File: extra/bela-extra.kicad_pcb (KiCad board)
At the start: 2 copper layers, 84 parts, among them P1 bbp9, P10 GU128x64E-U100, P11 gui140x16j-7002, P12 digital_in, P13 digital_out, P2 bbbp8, P3 enc+btn1, P4 enc+btn2, P5 MTA-156-4, P6 bela_power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

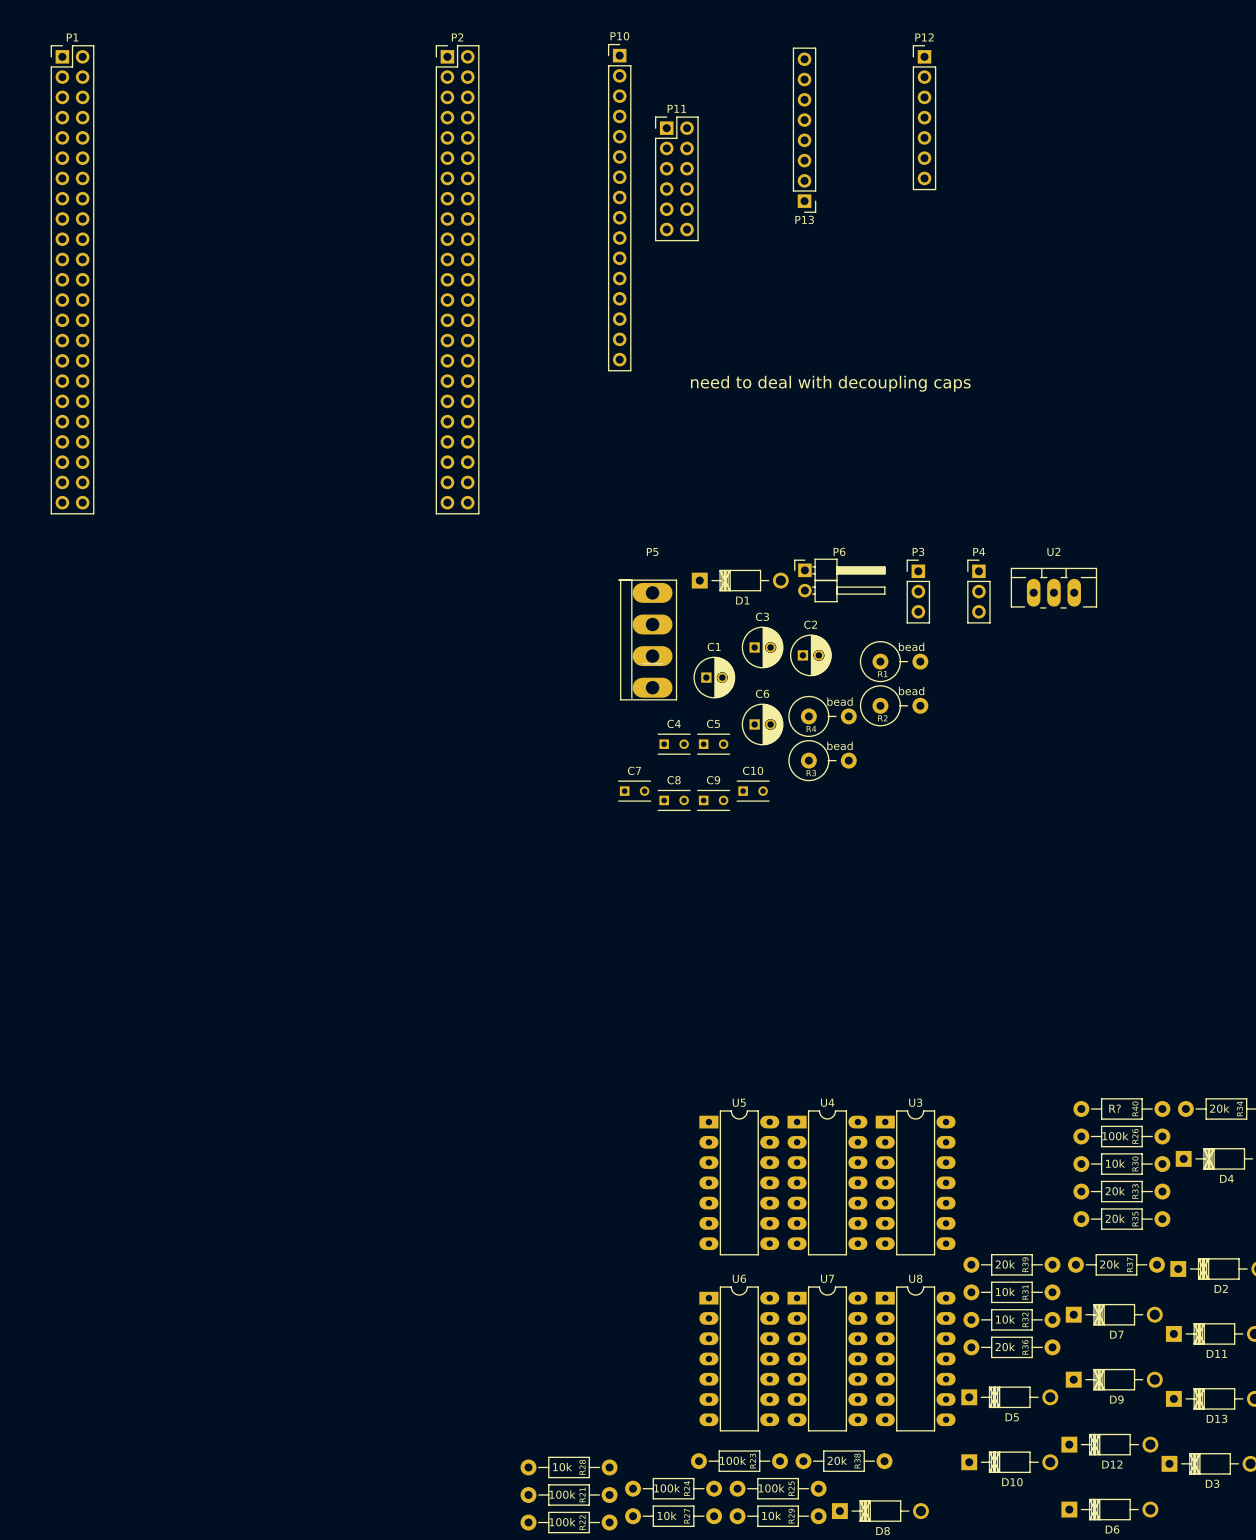
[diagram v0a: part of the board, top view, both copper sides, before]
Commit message: moving along, still no idea why 5v is hooked to 3.3v
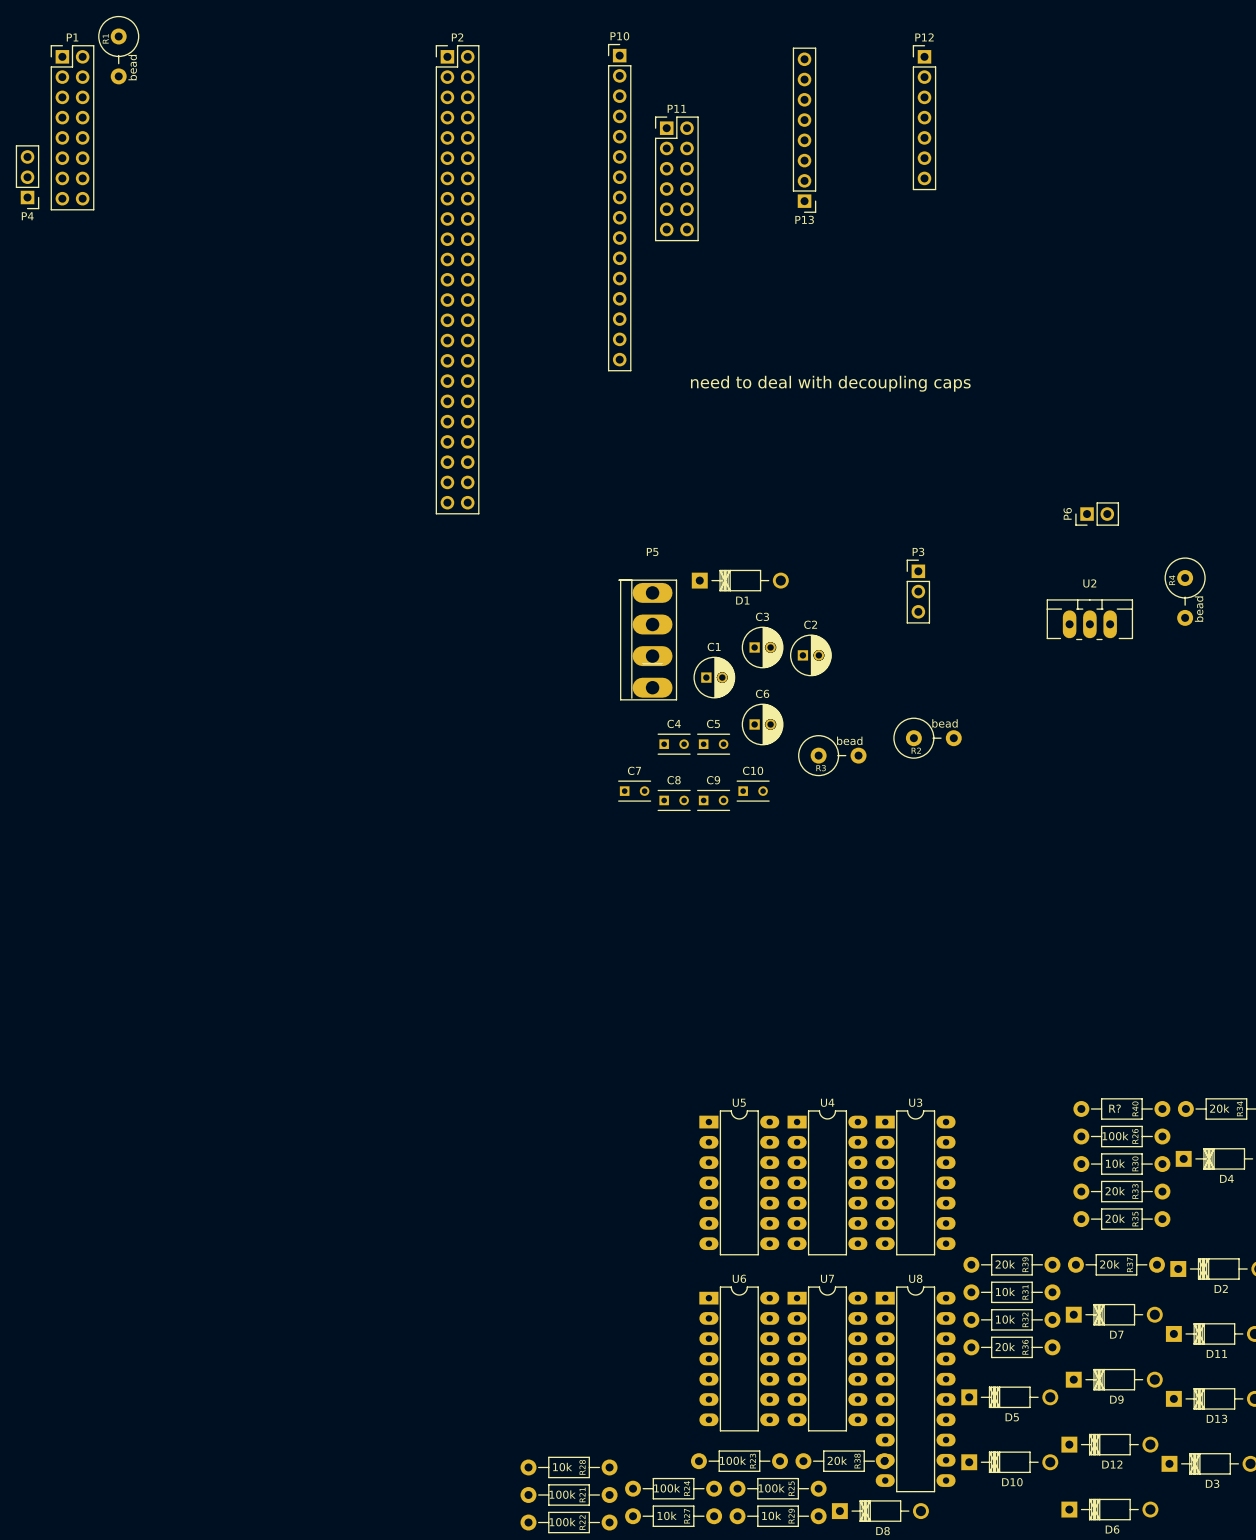
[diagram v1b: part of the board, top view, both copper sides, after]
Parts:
- P1: value bbp9 -> bbbp9; footprint Pin_Headers:Pin_Header_Straight_2x23_Pitch2.54mm -> Pin_Headers:Pin_Header_Straight_2x08_Pitch2.54mm
- P6: footprint Pin_Headers:Pin_Header_Angled_1x02_Pitch2.54mm -> Pin_Headers:Pin_Header_Straight_1x02_Pitch2.54mm
- U2: value LM78S05 -> 7805-xnor
- U8: footprint Housings_DIP:DIP-14_W7.62mm_LongPads -> Housings_DIP:DIP-20_W7.62mm_LongPads
- moved P4 128.1 mm to (21.0, 43.0), turned to 180 degrees
- moved R1 123.9 mm to (32.5, 25.3), turned to 270 degrees
- moved R4 47.1 mm to (166.1, 93.2), turned to 270 degrees
- moved P6 36.1 mm to (153.8, 82.7), turned to 90 degrees
- moved U2 5.99 mm to (154.2, 96.5)
- moved R2 5.83 mm to (134.6, 110.8)
- moved R3 1.37 mm to (122.7, 113.0)
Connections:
- net VSS renamed -15v
- C2 pad 1: 3.3v -> +15v
- C4 pad 1: 3.3v -> +15v
- C7 pad 1: 3.3v -> +15v
- C9 pad 1: 3.3v -> +15v
- D1 pad 2: 3.3v -> +15v
- P2 pad 10: (no net) -> beladigin4
- P2 pad 7: (no net) -> beladigin1
- P2 pad 8: (no net) -> beladigin2
- P2 pad 9: (no net) -> beladigin3
- R2 pad 2: 3.3v -> +15v
- U1 pad 4: 3.3v -> +15v
- U2 pad 1: (no net) -> Net-(C1-Pad1)
- U2 pad 2: (no net) -> GND
- U2 pad 3: (no net) -> 3.3v

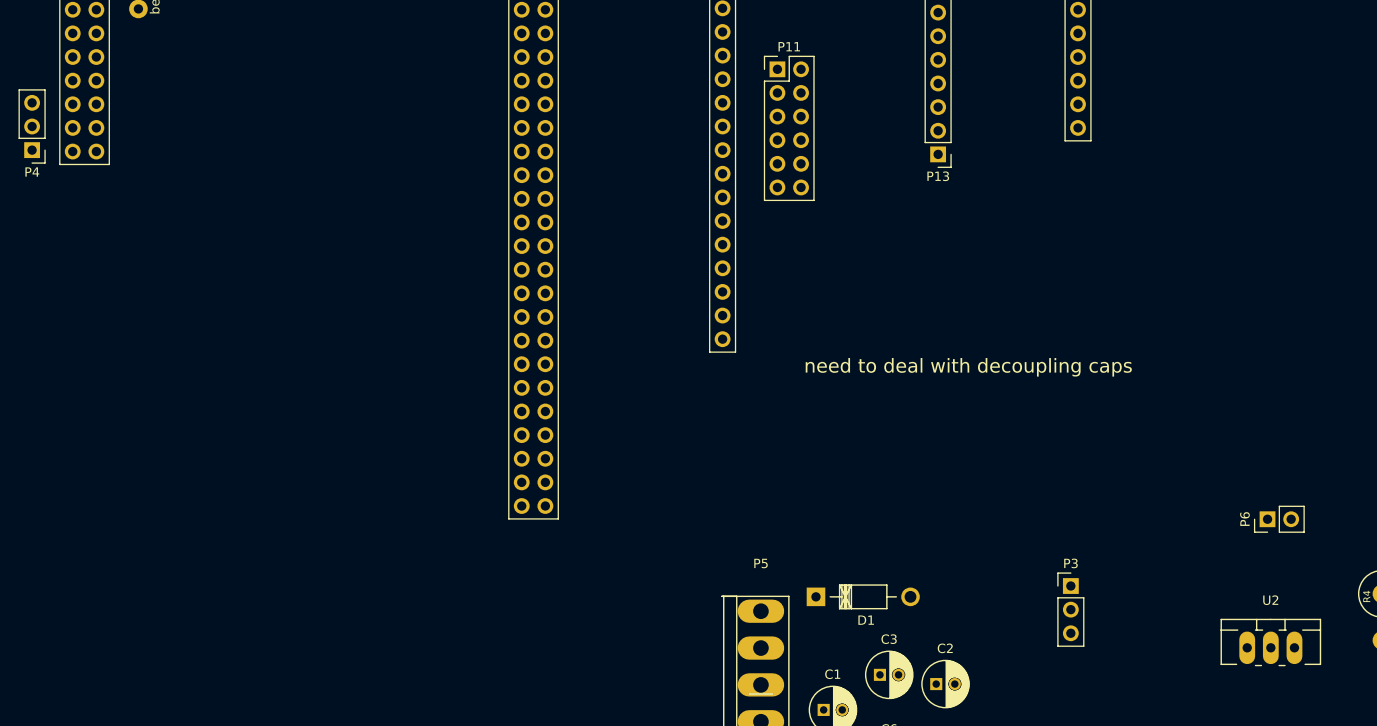
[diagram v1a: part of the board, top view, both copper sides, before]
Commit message: fixed up some footprint issues
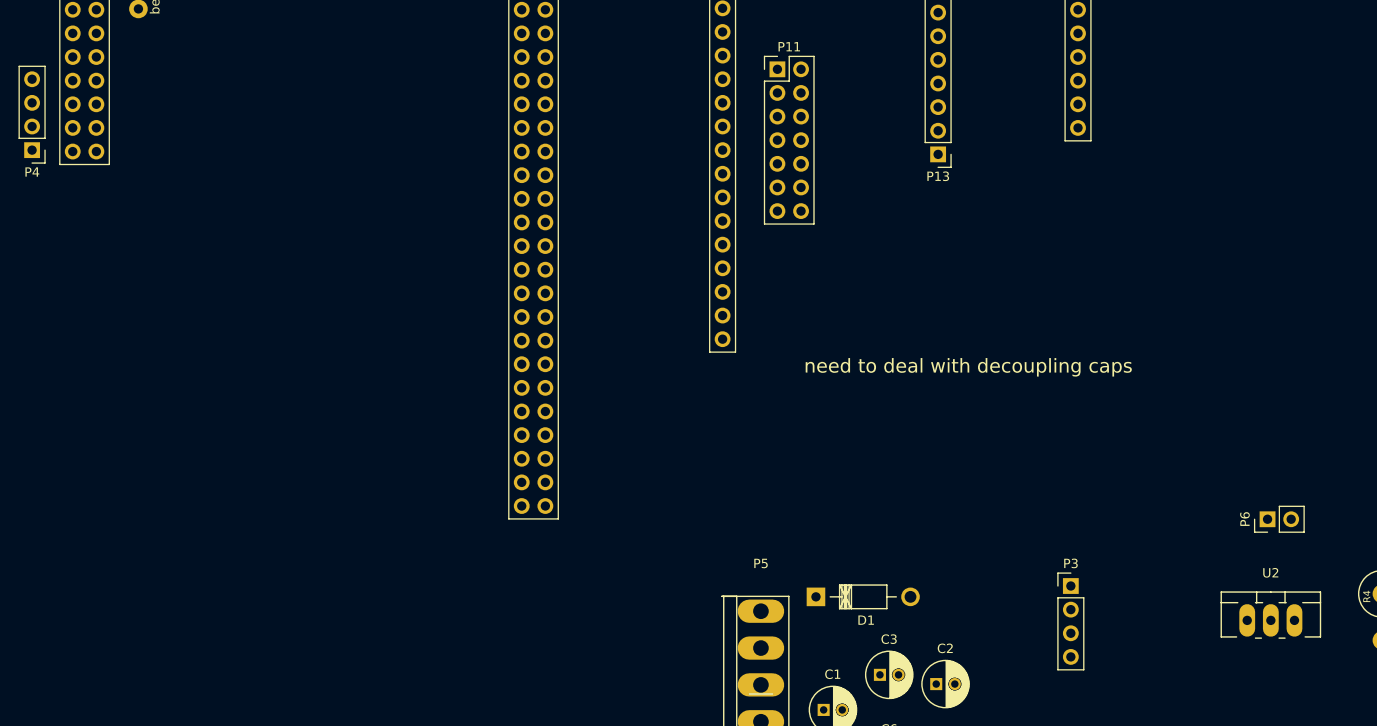
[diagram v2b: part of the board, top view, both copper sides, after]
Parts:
- P11: footprint Pin_Headers:Pin_Header_Straight_2x06_Pitch2.54mm -> Pin_Headers:Pin_Header_Straight_2x07_Pitch2.54mm
- P3, P4: footprint Pin_Headers:Pin_Header_Straight_1x03_Pitch2.54mm -> Pin_Headers:Pin_Header_Straight_1x04_Pitch2.54mm
- moved U2 2.95 mm to (154.2, 93.6)

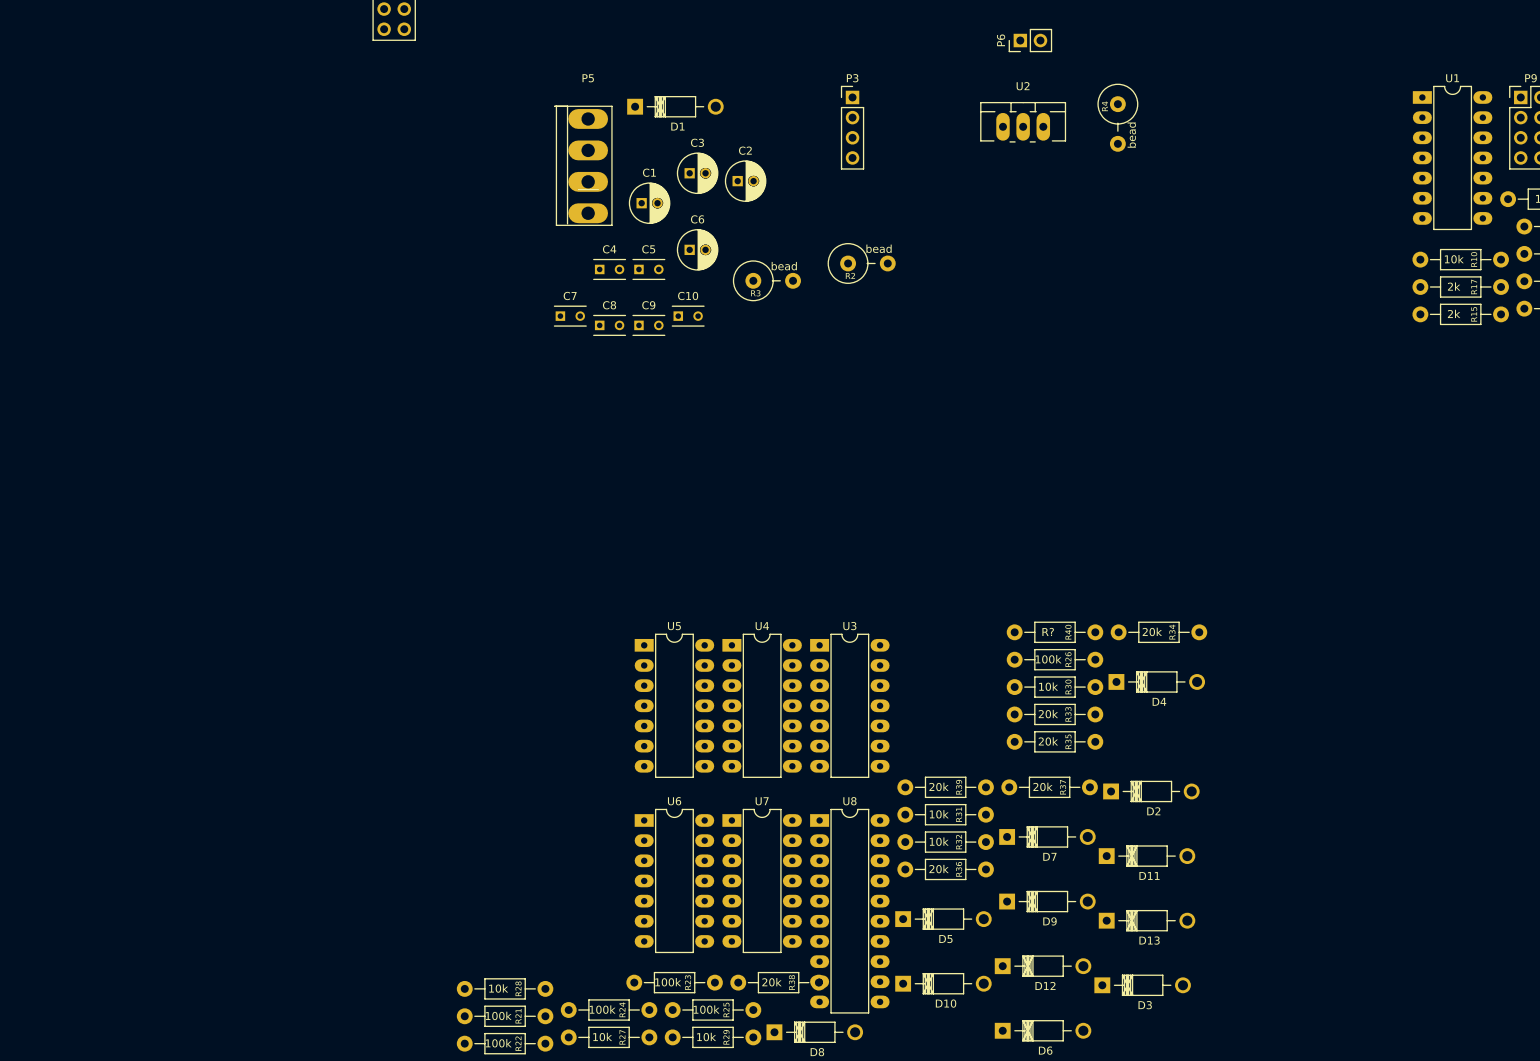
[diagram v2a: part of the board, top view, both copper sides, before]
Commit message: 3.3v is no longer connected to 5v!
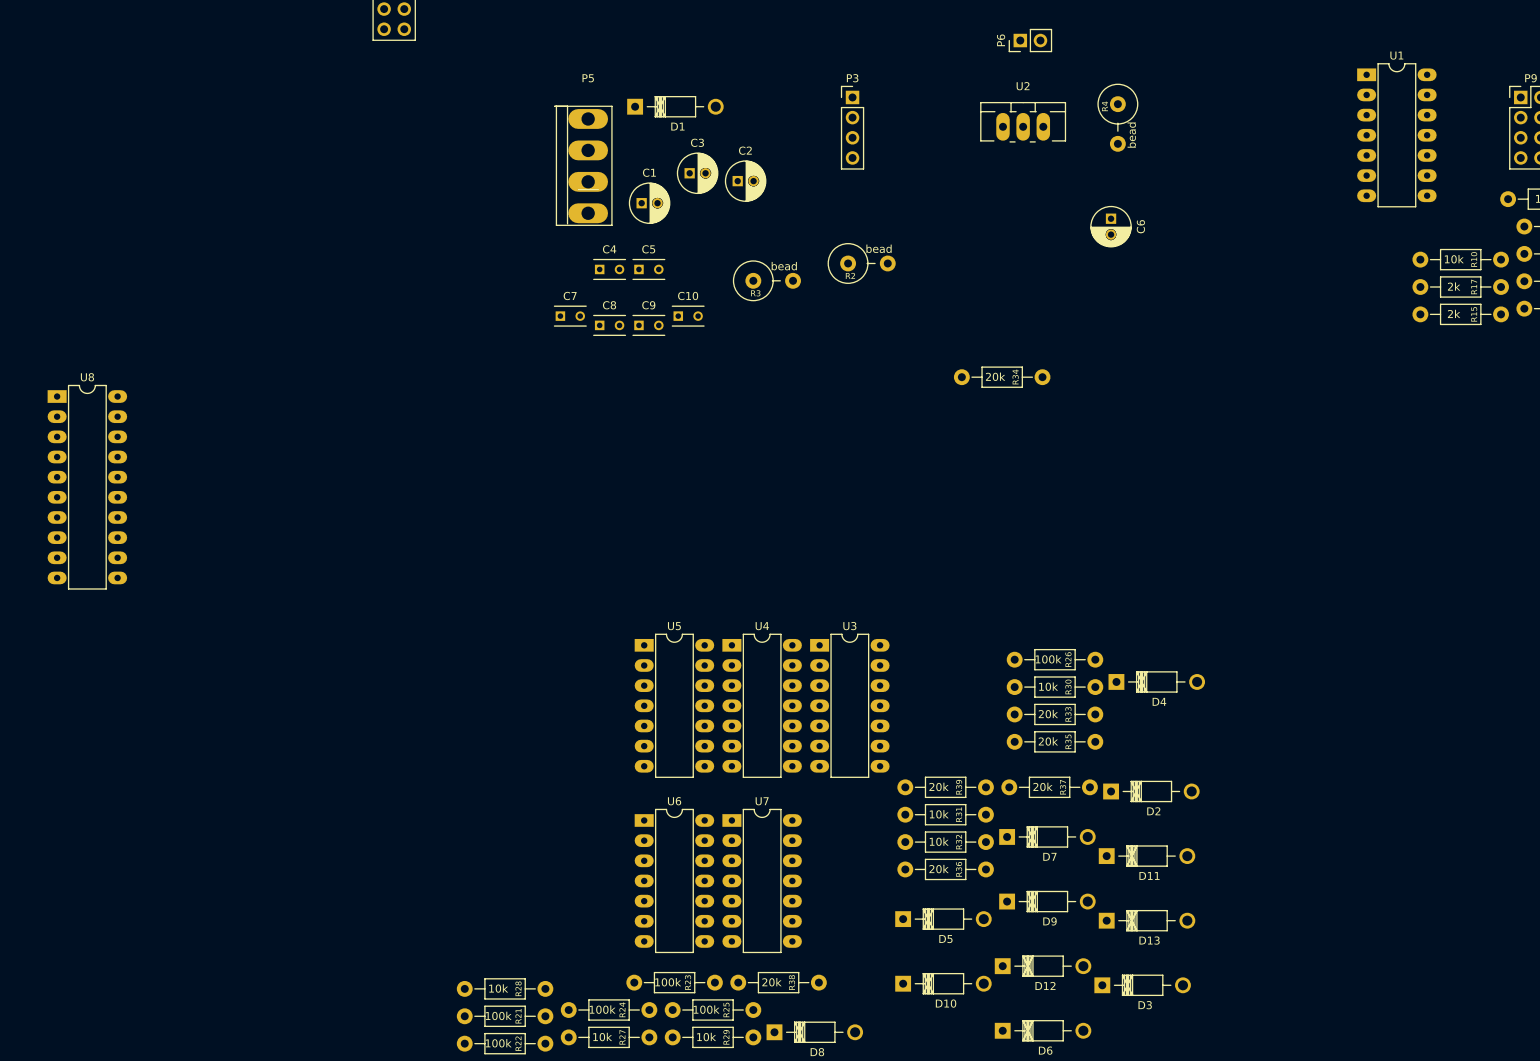
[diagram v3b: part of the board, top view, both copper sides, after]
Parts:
- removed R40: R?, xnorman:Resistor_Horizontal_RM10mm-xnorman
- U8: value 74LS245 -> 74LS245-xnor
- moved U8 109.9 mm to (32.5, 127.6)
- moved C6 53.2 mm to (165.3, 105.2), turned to 270 degrees
- moved R34 37.7 mm to (146.5, 125.1)
- moved U1 7.58 mm to (197.5, 87.0)
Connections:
- C6 pad 1: 3.3v -> 5v
- D10 pad 1: 3.3v -> 5v
- D12 pad 1: 3.3v -> 5v
- D2 pad 1: 3.3v -> 5v
- D4 pad 1: 3.3v -> 5v
- D6 pad 1: 3.3v -> 5v
- D8 pad 1: 3.3v -> 5v
- P10 pad 2: 3.3v -> 5v
- P11 pad 2: 3.3v -> 5v
- R4 pad 2: 3.3v -> 5v
- U2 pad 3: 3.3v -> 5v
- U3 pad 14: 3.3v -> 5v
- U4 pad 14: 3.3v -> 5v
- U5 pad 14: 3.3v -> 5v
- U6 pad 14: 3.3v -> 5v
- U7 pad 14: 3.3v -> 5v
- U8 pad 8: Net-(R40-Pad2) -> GND

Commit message: added decoupling caps, power expand, more layout
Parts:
- added C11: 10n, Capacitors_ThroughHole:C_Rect_L4_W2.5_P2.5, F.Cu at (131.2, 155.8)
- added C12: 10n, Capacitors_ThroughHole:C_Rect_L4_W2.5_P2.5, F.Cu at (70.2, 128.4)
- added P14: ext_power, Pin_Headers:Pin_Header_Straight_1x03_Pitch2.54mm, F.Cu at (21.2, 30.4)
- moved R9 220.9 mm to (13.0, 66.6)
- moved R5 219.7 mm to (18.2, 110.5)
- moved R11 211.6 mm to (17.5, 84.9), turned to 90 degrees
- moved P8 205.7 mm to (49.0, 114.2)
- moved R19 204.6 mm to (15.1, 60.5)
- moved R13 203.2 mm to (33.9, 93.9), turned to 180 degrees
- moved R7 200.5 mm to (17.9, 92.3), turned to 270 degrees
- moved R20 195.9 mm to (28.4, 75.8)
- moved R16 194.6 mm to (28.4, 59.3)
- moved R14 194.2 mm to (30.1, 106.1)
- moved R17 193.7 mm to (20.2, 53.3)
- moved P9 191.0 mm to (26.2, 101.7), turned to 90 degrees
- moved R15 186.6 mm to (30.7, 48.5)
- moved R18 186.4 mm to (38.6, 72.3), turned to 180 degrees
- moved P7 185.1 mm to (49.0, 103.4)
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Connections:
- C10 pad 1: GND -> 5v
- C10 pad 2: -15v -> GND
- C7 pad 1: +15v -> 5v
- C8 pad 1: GND -> 5v
- C8 pad 2: -15v -> GND
- C9 pad 1: +15v -> 5v
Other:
- board text removed: "need to deal with decoupling caps"
